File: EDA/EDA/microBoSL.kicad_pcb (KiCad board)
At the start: 4 copper layers, 45 x 15 mm, 55 parts, among them J1 Conn_01x04, J10 MOTOR_OUT, J11 Conn_01x03, J12 Conn_01x03, J13 Conn_01x03, J2 Conn_01x03, J3 Conn_01x04, J4 BATTERY CONN, J5 Conn_01x03, J6 Conn_01x04, J7 MOTOR_OUT, J8 USB_B_Micro, J9 MOTOR_OUT, Q1 DMP2165UW, SW1 RST_JMPR, SW2 AYZ0103AGRLC, U1 MAX40203ANS, U10 TPS709A33DBVT, U2 MAX40203ANS, U3 ATmega328P-MMH, U4 ZXBM5210-S, U5 74HC126PW-Q100, U6 MCP7940N-xSN, U7 FT232RQ, U8 ZXBM5210-S, U9 ZXBM5210-S, Y1 8MHz, Y2 32.768 kHz

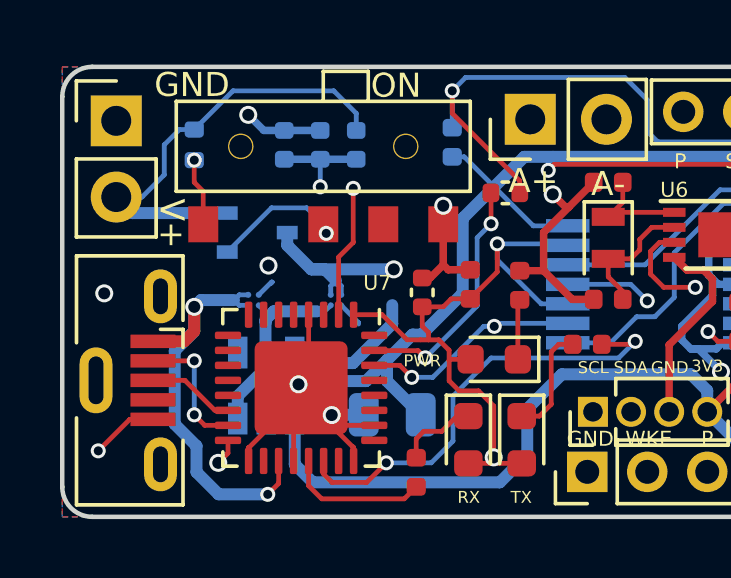
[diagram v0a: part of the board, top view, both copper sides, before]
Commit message: fixed o-ring circuit
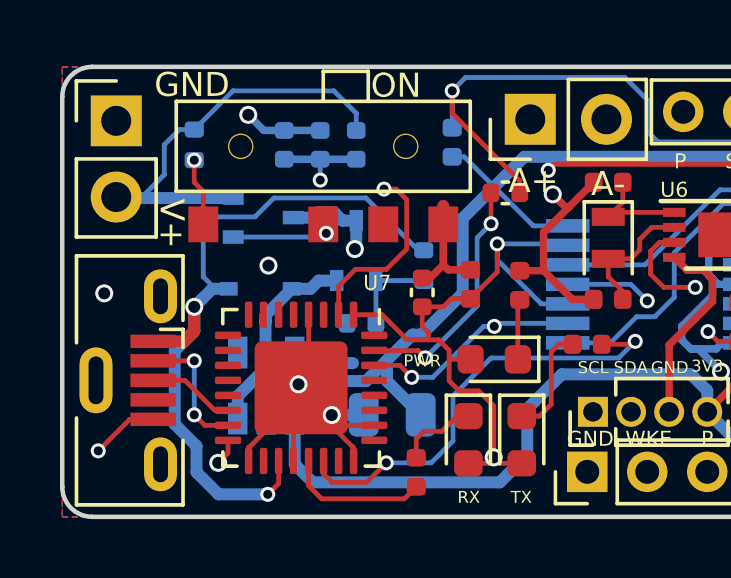
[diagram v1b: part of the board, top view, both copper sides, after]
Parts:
- removed U1, U2: MAX40203ANS, Package_BGA:WLP-4_0.73x0.73mm_Layout2x2_P0.35mm_Ball0.22mm_Pad0.2mm_NSMD
- added D4: CUS08F30,H3F, Diode_SMD:D_SOD-323, B.Cu at (106.6, 109.4)
- added Q2: DMP2165UW, Package_TO_SOT_SMD:SOT-323_SC-70, B.Cu at (109.8, 108.1)
- added R11: 10 kΩ, Resistor_SMD:R_0402_1005Metric, B.Cu at (112.0, 108.6)
- added R12: 4.7 MΩ, Capacitor_SMD:C_0402_1005Metric, B.Cu at (110.0, 110.5)
- moved Q1 0.54 mm to (106.7, 107.0)
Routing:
- net USB_V: track 14.9 -> 25.0 mm
- net GND: track 111.3 -> 107.3 mm, vias 14 -> 13
- net Net-(Q2-Pad1): track 0.00 -> 3.03 mm
- net VBAT: track 61.7 -> 60.2 mm
- net Net-(Q1-Pad1): track 4.38 -> 3.15 mm
- net AND_TX: track 18.7 -> 19.5 mm

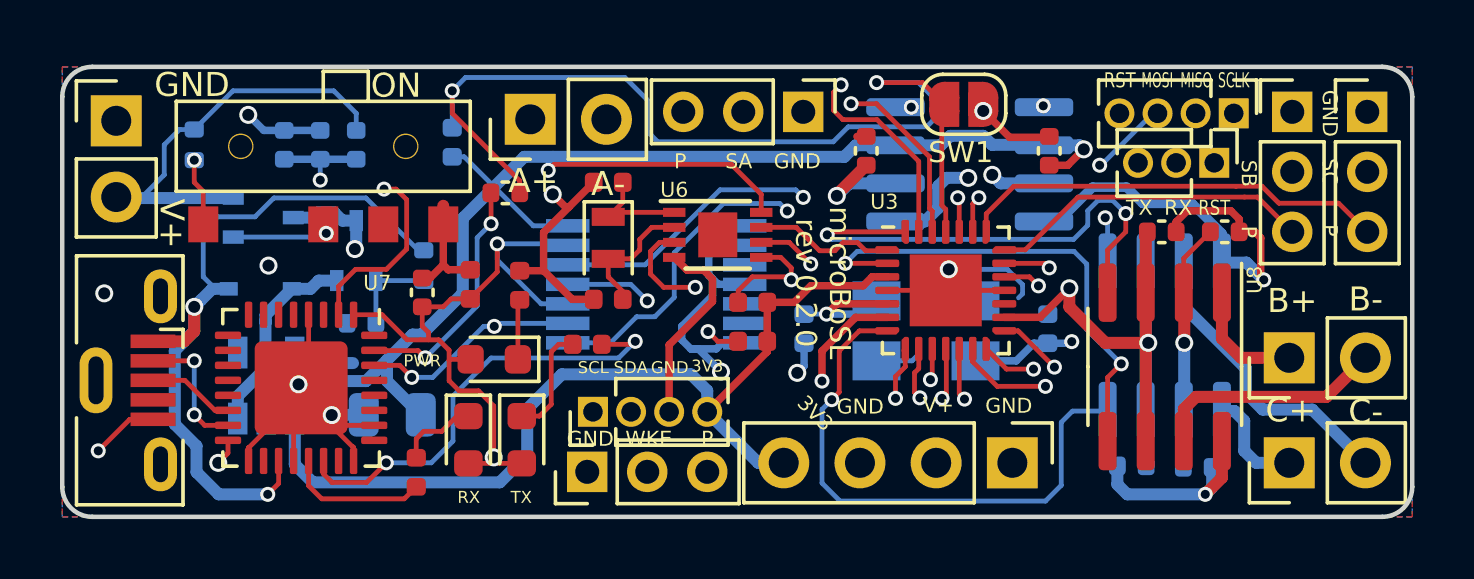
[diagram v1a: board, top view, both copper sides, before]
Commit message: rebase for adding wireless to microbosl
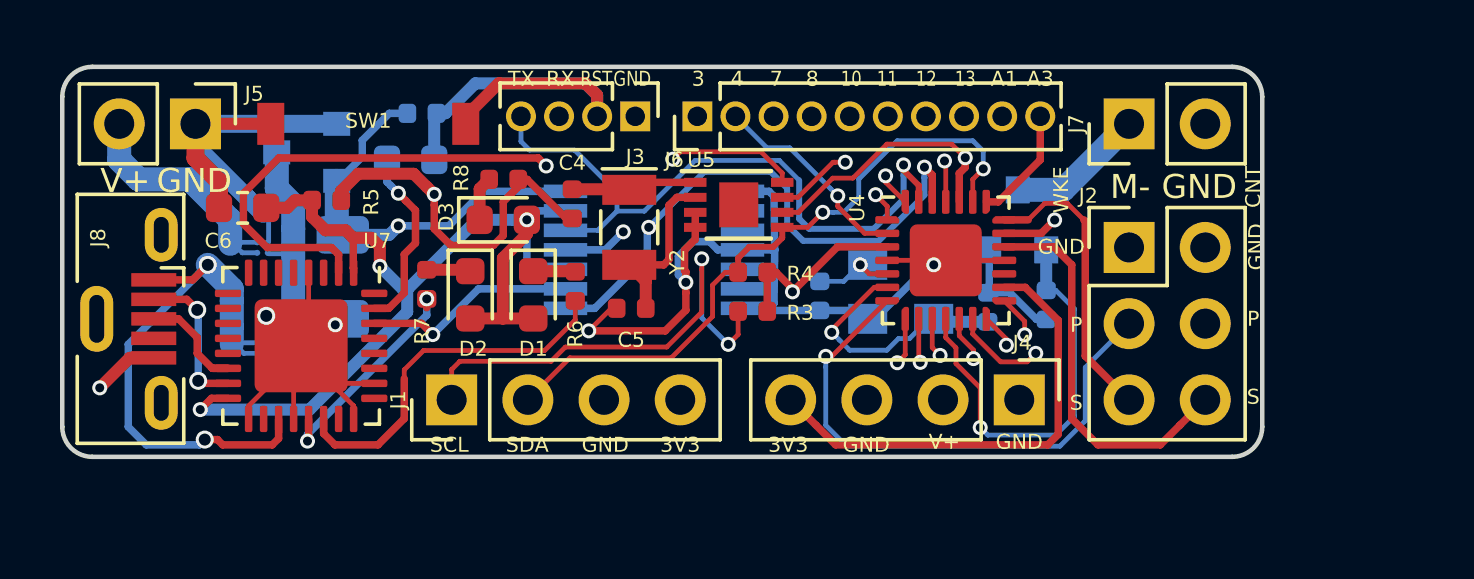
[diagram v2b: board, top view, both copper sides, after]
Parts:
- removed C10, C11, C12, C13, C14: 100 nF, Capacitor_SMD:C_0402_1005Metric
- removed C8, C9: 15 pF, Capacitor_SMD:C_0402_1005Metric
- removed D4: CUS08F30,H3F, Diode_SMD:D_SOD-323
- removed J10, J9: MOTOR_OUT, Connector_PinHeader_2.54mm:PinHeader_1x02_P2.54mm_Vertical
- removed J11, J12, J13: Conn_01x03, Connector_PinHeader_2.00mm:PinHeader_1x03_P2.00mm_Vertical
- removed Q2: DMP2165UW, Package_TO_SOT_SMD:SOT-323_SC-70
- removed R10, R9: 3.3 kΩ, Resistor_SMD:R_0402_1005Metric
- removed R11: 10 kΩ, Resistor_SMD:R_0402_1005Metric
- removed R12: 4.7 MΩ, Capacitor_SMD:C_0402_1005Metric
- removed SW2: AYZ0103AGRLC, SIMFootprints:AYZ0103AGRLC
- removed U10: TPS709A33DBVT, Package_TO_SOT_SMD:SOT-23-5
- removed U8, U9: ZXBM5210-S, Package_SO:SOIC-8_3.9x4.9mm_P1.27mm
- added U1: MAX40200ANS, Package_BGA:WLP-4_0.73x0.73mm_Layout2x2_P0.35mm_Ball0.22mm_Pad0.2mm_NSMD, B.Cu at (106.7, 111.4)
- added U2: MAX40200ANS, Package_BGA:WLP-4_0.73x0.73mm_Layout2x2_P0.35mm_Ball0.22mm_Pad0.2mm_NSMD, B.Cu at (106.7, 108.0)
- C1: value 2.2 μF -> 1 μF; footprint Capacitor_SMD:C_0805_2012Metric -> Capacitor_SMD:C_1206_3216Metric
- C2, C3: value 100 nF -> 22 pF; moved to B.Cu
- C4: value 100 nF -> 12 pF
- C5: value 15 pF -> 12 pF; moved to F.Cu
- C6: value 15 pF -> 100 nF; footprint Capacitor_SMD:C_0402_1005Metric -> Capacitor_SMD:C_0603_1608Metric; moved to F.Cu
- C7: footprint Capacitor_SMD:C_0402_1005Metric -> Capacitor_SMD:C_0603_1608Metric
- J1: footprint Connector_PinHeader_1.27mm:PinHeader_1x04_P1.27mm_Vertical -> Connector_PinHeader_2.54mm:PinHeader_1x04_P2.54mm_Vertical
- J2: value Conn_01x03 -> Conn_02x03_Odd_Even; footprint Connector_PinHeader_1.27mm:PinHeader_1x03_P1.27mm_Vertical -> Connector_PinHeader_2.54mm:PinHeader_2x03_P2.54mm_Vertical
- J3: footprint Connector_PinHeader_2.54mm:PinHeader_1x04_P2.54mm_Vertical -> Connector_PinHeader_1.27mm:PinHeader_1x04_P1.27mm_Vertical
- J4: value BATTERY CONN -> Conn_01x04; footprint Connector_PinHeader_2.54mm:PinHeader_1x02_P2.54mm_Vertical -> Connector_PinHeader_2.54mm:PinHeader_1x04_P2.54mm_Vertical
- J5: value Conn_01x03 -> Conn_01x02; footprint Connector_PinHeader_2.00mm:PinHeader_1x03_P2.00mm_Vertical -> Connector_PinHeader_2.54mm:PinHeader_1x02_P2.54mm_Vertical
- J6: value Conn_01x04 -> Conn_01x10; footprint Connector_PinHeader_1.27mm:PinHeader_1x04_P1.27mm_Vertical -> Connector_PinHeader_1.27mm:PinHeader_1x10_P1.27mm_Vertical
- J7: value MOTOR_OUT -> Conn_01x02
- Q1: value DMP2165UW -> DMG2302UK; footprint Package_TO_SOT_SMD:SOT-323_SC-70 -> Package_TO_SOT_SMD:SOT-23
- R2: value 10 kΩ -> 1 kΩ
- R5: value 4.7 MΩ -> 10 kΩ; footprint Capacitor_SMD:C_0402_1005Metric -> Resistor_SMD:R_0402_1005Metric; moved to F.Cu
- R6: value 4.7 MΩ -> 3.3 kΩ; footprint Capacitor_SMD:C_0402_1005Metric -> Resistor_SMD:R_0402_1005Metric; moved to F.Cu
- R7: value 10 kΩ -> 3.3 kΩ
- SW1: value RST_JMPR -> PTS636 SM43J SMTR LFS; footprint Jumper:SolderJumper-2_P1.3mm_Open_RoundedPad1.0x1.5mm -> SIMFootprints:PTS636 SM43J SMTR LFS
- U3: value ATmega328P-MMH -> MCP1700-3302E_SOT23; footprint Package_DFN_QFN:QFN-28-1EP_4x4mm_P0.45mm_EP2.4x2.4mm -> Package_TO_SOT_SMD:SOT-23; moved to B.Cu
- U4: value ZXBM5210-S -> ATmega328-MMH; footprint Package_SO:SOIC-8_3.9x4.9mm_P1.27mm -> Package_DFN_QFN:QFN-28-1EP_4x4mm_P0.45mm_EP2.4x2.4mm; moved to F.Cu
- U5: value 74HC126PW-Q100 -> MCP7940N-xSN; footprint Package_SO:TSSOP-14_4.4x5mm_P0.65mm -> Package_DFN_QFN:DFN-8-1EP_3x2mm_P0.5mm_EP1.3x1.5mm; moved to F.Cu
- U6: value MCP7940N-xSN -> 74HC126PW-Q100; footprint Package_DFN_QFN:DFN-8-1EP_3x2mm_P0.5mm_EP1.3x1.5mm -> Package_SO:TSSOP-14_4.4x5mm_P0.65mm; moved to B.Cu
- Y1: footprint Crystal:Crystal_SMD_5032-4Pin_5.0x3.2mm -> Crystal:Crystal_SMD_EuroQuartz_MT-4Pin_3.2x2.5mm
- Y2: footprint Crystal:Crystal_SMD_2012-2Pin_2.0x1.2mm -> Crystal:Crystal_SMD_EuroQuartz_EQ161-2Pin_3.2x1.5mm
- moved J4 31.5 mm to (131.9, 113.1), turned to 270 degrees
- moved C6 27.1 mm to (106.0, 106.7), turned to 180 degrees
- moved Q1 25.2 mm to (131.8, 107.1), turned to 90 degrees
- moved U3 21.8 mm to (108.2, 104.8), turned to 180 degrees
- moved R2 20.5 mm to (132.8, 109.9)
- moved J7 20.0 mm to (135.6, 103.9)
- moved SW1 19.9 mm to (110.2, 103.9)
- moved J6 17.9 mm to (121.2, 103.7), turned to 90 degrees
- moved J5 17.5 mm to (104.4, 103.9), turned to 270 degrees
- moved J3 17.1 mm to (119.1, 103.7)
- moved R6 10.8 mm to (117.1, 109.3), turned to 270 degrees
- moved C4 9.96 mm to (117.0, 106.6)
- moved C3 9.05 mm to (125.2, 109.6), turned to 90 degrees
- moved R1 7.66 mm to (112.0, 103.5), turned to 0 degrees
- moved D3 7.42 mm to (114.7, 107.1), turned to 0 degrees
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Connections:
- C2 pad 2: V_3.3 -> Net-(C2-Pad2)
- C3 pad 2: V_3.3 -> Net-(C3-Pad2)
- C4 pad 1: VBAT -> GND
- C4 pad 2: GND -> Net-(C4-Pad2)
- C6 pad 1: GND -> TTL_3.3V
- C6 pad 2: Net-(C6-Pad2) -> GND
- C7 pad 1: Net-(C7-Pad1) -> TLL_RST
- C7 pad 2: GND -> Net-(C7-Pad2)
- J2 pad 1: TLL_RST -> GND
- J2 pad 2: TLL_RX -> GND
- J2 pad 3: TLL_TX -> Hall_WKE_P
- J3 pad 2: VBAT -> TLL_RST
- J3 pad 3: GND -> TLL_RX
- J3 pad 4: V_3.3 -> TLL_TX
- J5 pad 1: Hall_WKE_S -> GND
- J5 pad 2: GND -> VPP
- J6 pad 1: SCLK -> D3
- J6 pad 2: MISO -> D4
- J6 pad 3: MOSI -> D7
- J6 pad 4: TLL_RST -> D8
- J7 pad 2: Net-(J7-Pad2) -> GND
- Q1 pad 1: Net-(Q1-Pad1) -> MOSFET
- Q1 pad 2: VPP -> GND
- Q1 pad 3: VBAT -> Net-(J7-Pad1)
- R1 pad 1: Net-(R1-Pad1) -> V_3.3
- R1 pad 2: VPP -> TLL_RST
- R2 pad 1: V_3.3 -> GND
- R2 pad 2: TLL_RST -> MOSFET
- R3 pad 1: V_3.3 -> SCL
- R3 pad 2: SDA -> V_3.3
- R4 pad 1: SCL -> V_3.3
- R4 pad 2: V_3.3 -> SDA
- R5 pad 1: VPP -> TTL_3.3V
- R5 pad 2: Net-(C7-Pad1) -> GND
- R6 pad 1: Net-(C7-Pad1) -> Net-(D1-Pad1)
- R6 pad 2: GND -> Net-(R6-Pad2)
- R7 pad 1: TTL_3.3V -> Net-(D2-Pad1)
- R7 pad 2: GND -> Net-(R7-Pad2)
- R8 pad 1: Net-(D2-Pad1) -> Net-(D3-Pad1)
- R8 pad 2: Net-(R8-Pad2) -> GND
- U3 pad 1: RTC_I -> GND
- U3 pad 2: MREV_B -> V_3.3
- U3 pad 3: V_3.3 -> Net-(U1-PadA2)
- U4 pad 1: Net-(J7-Pad1) -> D3
- U4 pad 2: VBAT -> D4
- U4 pad 4: MFWD_A -> GND
- U4 pad 5: MREV_A -> Net-(C3-Pad2)
- U4 pad 6: V_3.3 -> Net-(C2-Pad2)
- U4 pad 7: Net-(J7-Pad2) -> Hall_WKE_P
- U4 pad 8: GND -> Hall_CNT_P
- U5 pad 1: GND -> Net-(C4-Pad2)
- U5 pad 2: Net-(U5-Pad2) -> Net-(C5-Pad2)
- U5 pad 3: Net-(U5-Pad3) -> GND
- U5 pad 5: Net-(U5-Pad5) -> SDA
- U5 pad 6: Net-(U5-Pad6) -> SCL
- U5 pad 7: GND -> RTC_I
- U5 pad 8: TLL_RX -> V_3.3
- U5 pad 9: AND_RX -> (no net)
- U6 pad 1: Net-(C9-Pad2) -> GND
- U6 pad 2: Net-(C8-Pad2) -> Net-(U6-Pad2)
- U6 pad 3: Net-(C7-Pad1) -> Net-(U6-Pad3)
- U6 pad 5: SDA -> Net-(U6-Pad5)
- U6 pad 6: SCL -> Net-(U6-Pad6)
- U6 pad 7: RTC_I -> GND
- U6 pad 8: V_3.3 -> TLL_RX
- U6 pad 9: (no net) -> AND_RX
- U7 pad 21: Net-(R9-Pad2) -> Net-(R7-Pad2)
- U7 pad 22: Net-(R8-Pad2) -> Net-(R6-Pad2)
- U7 pad 31: Net-(C11-Pad2) -> Net-(C7-Pad2)
- Y1 pad 1: Net-(C6-Pad2) -> Net-(C2-Pad2)
- Y1 pad 3: Net-(C5-Pad2) -> Net-(C3-Pad2)
- Y2 pad 1: Net-(C9-Pad2) -> Net-(C4-Pad2)
- Y2 pad 2: Net-(C8-Pad2) -> Net-(C5-Pad2)
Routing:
- net VBAT: track 60.2 -> 0.00 mm, vias 3 -> 0
- net V_3.3: track 105.4 -> 65.0 mm, vias 4 -> 3
- net VPP: track 15.4 -> 43.6 mm
- net GND: track 107.3 -> 81.0 mm, vias 13 -> 7
- net Hall_P: track 24.3 -> 0.00 mm, vias 1 -> 0
- net Hall_P2: track 23.7 -> 0.00 mm, vias 1 -> 0
- net Net-(C7-Pad1): track 20.6 -> 0.00 mm, vias 2 -> 0
- net Hall_CNT_P: track 0.00 -> 19.7 mm, vias 0 -> 1
- net Hall_WKE_P: track 0.00 -> 18.8 mm, vias 0 -> 1
- net MFWD_C: track 18.8 -> 0.00 mm, vias 1 -> 0
- net SCLK: track 16.9 -> 0.00 mm, vias 1 -> 0
- net TLL_RST: track 47.3 -> 30.6 mm, vias 2 -> 1
- net MFWD_B: track 16.5 -> 0.00 mm, vias 2 -> 0
- net MREV_A: track 16.4 -> 0.00 mm, vias 2 -> 0
- net MREV_B: track 16.4 -> 0.00 mm, vias 2 -> 0
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- removed copper zone on B.Cu, net GND
- removed copper zone on F.Cu, net GND
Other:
- board size 45 x 15 mm -> 40 x 13 mm
- board text added: "10"
- board text added: "11"
- board text added: "12"
- board text added: "13"
- board text added: "3"
- board text added: "4"
- board text added: "7"
- board text added: "8"
- board text added: "A1"
- board text added: "A3"
- board text added: "CNT"
- board text added: "M-"
- board text added: "S"
- board text added: "microBoSL rev 0.1.0"
- board text removed: "A+"
- board text removed: "A-"
- board text removed: "B+"
- board text removed: "B-"
- board text removed: "C+"
- board text removed: "C-"
- board text removed: "MISO"
- board text removed: "MOSI"
- board text removed: "ON"
- board text removed: "PWR"
- board text removed: "SA"
- board text removed: "SB"
- board text removed: "SC"
- board text removed: "SCLK"
- board text removed: "microBoSL rev 0.2.0"

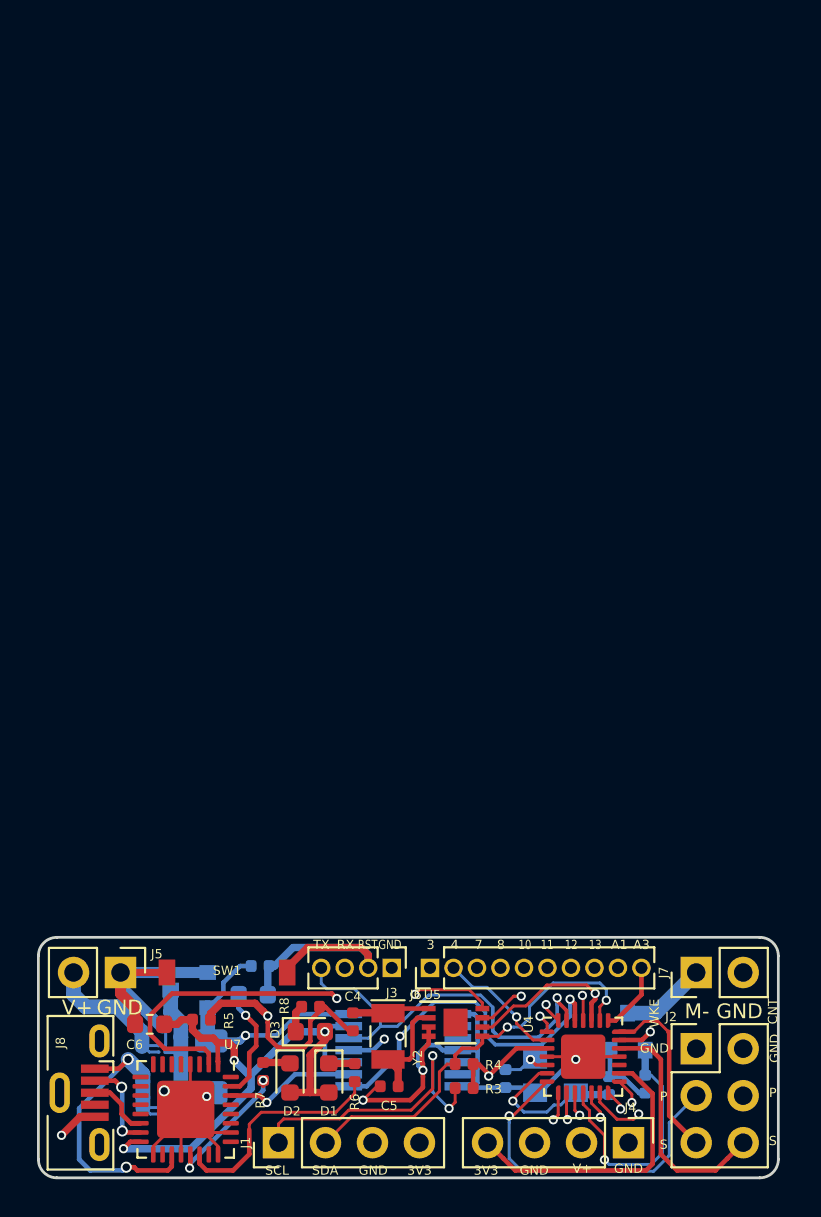
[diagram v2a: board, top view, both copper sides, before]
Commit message: added Si4463 radio module
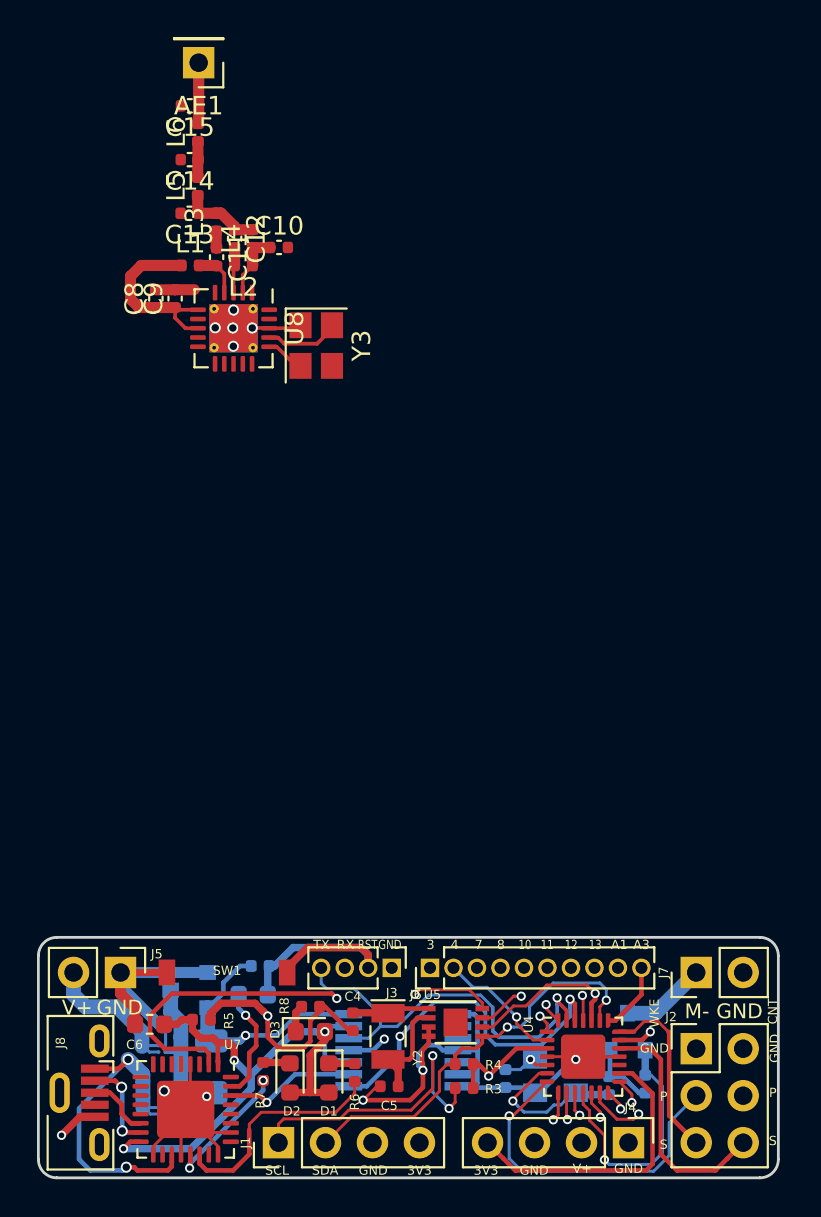
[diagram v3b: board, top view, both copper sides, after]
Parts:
- added AE1: Antenna, Connector_PinHeader_2.54mm:PinHeader_1x01_P2.54mm_Vertical, F.Cu at (108.7, 54.7)
- added C10: C, Capacitor_SMD:C_0402_1005Metric, F.Cu at (113.0, 64.7)
- added C11: C, Capacitor_SMD:C_0402_1005Metric, F.Cu at (109.6, 65.2)
- added C12: C, Capacitor_SMD:C_0402_1005Metric, F.Cu at (110.6, 64.2)
- added C13: C, Capacitor_SMD:C_0402_1005Metric, F.Cu at (108.2, 62.9)
- added C14: C, Capacitor_SMD:C_0402_1005Metric, F.Cu at (108.2, 60.0)
- added C15: C, Capacitor_SMD:C_0402_1005Metric, F.Cu at (108.2, 57.0)
- added C8: 100 pF, Capacitor_SMD:C_0402_1005Metric, F.Cu at (106.3, 67.5)
- added C9: 100 nF, Capacitor_SMD:C_0402_1005Metric, F.Cu at (107.4, 67.5)
- added L1: L, Inductor_SMD:L_0402_1005Metric, F.Cu at (108.2, 65.7)
- added L2: L, Inductor_SMD:L_0402_1005Metric, F.Cu at (111.1, 65.7)
- added L3: L, Inductor_SMD:L_0402_1005Metric, F.Cu at (109.6, 63.3)
- added L4: L, Inductor_SMD:L_0402_1005Metric, F.Cu at (111.6, 64.2)
- added L5: L, Inductor_SMD:L_0402_1005Metric, F.Cu at (108.6, 61.4)
- added L6: L, Inductor_SMD:L_0402_1005Metric, F.Cu at (108.6, 58.5)
- added U8: Si4463, Package_DFN_QFN:QFN-20-1EP_4x4mm_P0.5mm_EP2.6x2.6mm_ThermalVias, F.Cu at (110.5, 69.1)
- added Y3: 30 MHz, Crystal:Crystal_SMD_Abracon_ABM8G-4Pin_3.2x2.5mm, F.Cu at (115.0, 70.0)
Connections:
- J6 pad 1: D3 -> unconnected-(J6-Pad1)
- J6 pad 2: D4 -> unconnected-(J6-Pad2)
- J6 pad 5: D10 -> unconnected-(J6-Pad5)
- J6 pad 6: D11 -> unconnected-(J6-Pad6)
- J6 pad 7: D12 -> unconnected-(J6-Pad7)
- J6 pad 8: D13 -> unconnected-(J6-Pad8)
- J8 pad 4: Net-(J8-Pad4) -> unconnected-(J8-Pad4)
- J8 pad 6: (no net) -> unconnected-(J8-Pad6)
- U4 pad 1: D3 -> I_RADIO
- U4 pad 12: D10 -> SS
- U4 pad 13: D11 -> MOSI
- U4 pad 14: D12 -> MISO
- U4 pad 15: D13 -> SCLK
- U4 pad 2: D4 -> EN_RADIO
- U6 pad 2: Net-(U6-Pad2) -> unconnected-(U6-Pad2)
- U6 pad 3: Net-(U6-Pad3) -> unconnected-(U6-Pad3)
- U6 pad 5: Net-(U6-Pad5) -> unconnected-(U6-Pad5)
- U6 pad 6: Net-(U6-Pad6) -> unconnected-(U6-Pad6)
- U7 pad 10: Net-(U7-Pad10) -> unconnected-(U7-Pad10)
- U7 pad 11: Net-(U7-Pad11) -> unconnected-(U7-Pad11)
- U7 pad 18: Net-(U7-Pad18) -> unconnected-(U7-Pad18)
- U7 pad 27: Net-(U7-Pad27) -> unconnected-(U7-Pad27)
- U7 pad 28: Net-(U7-Pad28) -> unconnected-(U7-Pad28)
- U7 pad 3: Net-(U7-Pad3) -> unconnected-(U7-Pad3)
- U7 pad 32: Net-(U7-Pad32) -> unconnected-(U7-Pad32)
- U7 pad 33: GND -> (no net)
- U7 pad 6: Net-(U7-Pad6) -> unconnected-(U7-Pad6)
- U7 pad 7: Net-(U7-Pad7) -> unconnected-(U7-Pad7)
- U7 pad 8: Net-(U7-Pad8) -> unconnected-(U7-Pad8)
- U7 pad 9: Net-(U7-Pad9) -> unconnected-(U7-Pad9)
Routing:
- net MOSI: track 0.00 -> 15.0 mm, vias 0 -> 1
- net D11: track 15.0 -> 0.00 mm, vias 1 -> 0
- net SS: track 0.00 -> 13.1 mm, vias 0 -> 1
- net D10: track 13.1 -> 0.00 mm, vias 1 -> 0
- net MISO: track 0.00 -> 10.4 mm, vias 0 -> 1
- net D12: track 10.4 -> 0.00 mm, vias 1 -> 0
- net V_3.3: track 65.0 -> 75.2 mm
- net SCLK: track 0.00 -> 9.64 mm, vias 0 -> 1
- net D13: track 9.64 -> 0.00 mm, vias 1 -> 0
- net I_RADIO: track 0.00 -> 8.80 mm, vias 0 -> 1
- net D3: track 8.80 -> 0.00 mm, vias 1 -> 0
- net EN_RADIO: track 0.00 -> 6.88 mm, vias 0 -> 1
- net D4: track 6.88 -> 0.00 mm, vias 1 -> 0
- net GND: track 81.0 -> 85.8 mm, vias 7 -> 12
- net Net-(C12-Pad1): track 0.00 -> 4.40 mm
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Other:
- net class Default removed
- net class Power removed
- net class RF removed
